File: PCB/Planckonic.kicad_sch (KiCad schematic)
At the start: 127 parts

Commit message: schematic improvements
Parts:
- gave numbers to parts that had none: 127
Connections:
- net col0: now also SW_A9.1, SW_C9.1, U1.5 (2/PD1)
- net col1: now also SW_A10.1, SW_C10.1, U1.6 (3/PD0)
- net col2: now also SW_A11.1, SW_C11.1, U1.7 (4/PD4)
- net col3: now also SW_A12.1, SW_C12.1, U1.8 (5/PC6)
- net col4: now also SW_B9.1, SW_D12.1, SW_E12.1, U1.9 (6/PD7)
- net col5: now also SW_B10.1, SW_D13.1, SW_E13.1, U1.10 (7/PE6)
- net col6: now also SW_B11.1, SW_D14.1, SW_E14.1, U1.11 (8/PB4)
- net col7: now also SW_B12.1, SW_D15.1, SW_E15.1, U1.12 (9/PB5)
- net rowA: now also U1.20 (A3/PF4); no longer D10.2 (A), D11.2 (A), D12.2 (A), D9.2 (A)
- net rowB: now also U1.19 (A2/PF5); no longer D21.2 (A), D22.2 (A), D23.2 (A), D24.2 (A)
- net rowC: now also U1.18 (A1/PF6); no longer D25.2 (A), D34.2 (A), D35.2 (A), D36.2 (A)
- net rowD: now also U1.17 (A0/PF7); no longer D37.2 (A), D38.2 (A), D46.2 (A), D47.2 (A)
- net rowE: now also D10.2 (A), D11.2 (A), D12.2 (A), D21.2 (A), D22.2 (A), D23.2 (A), D24.2 (A), D9.2 (A), U1.16 (15/PB1); no longer D49.2 (A), D50.2 (A), D51.2 (A), D52.2 (A), D53.2 (A), D54.2 (A), D55.2 (A), D56.2 (A), D57.2 (A), D58.2 (A), D59.2 (A), D60.2 (A)
- net rowH: now reaches U1.13 (10/PB6)
- net rowH: now also D49.2 (A), D58.2 (A), D59.2 (A), D60.2 (A)
- net rowG: now reaches U1.14 (16/PB2)
- net rowG: now also D50.2 (A), D51.2 (A), D52.2 (A), D53.2 (A), D54.2 (A), D55.2 (A), D56.2 (A), D57.2 (A)
- net rowF: now reaches U1.15 (14/PB3)
- net rowF: now also D25.2 (A), D34.2 (A), D35.2 (A), D36.2 (A), D37.2 (A), D38.2 (A), D46.2 (A), D47.2 (A)
- net VCC: now reaches U1.21 (VCC)
- net GND: now reaches U1.23 (GND)
- net GND: now also U1.3 (GND), U1.4 (GND)
- removed net col10: SW_A11.1, SW_B11.1, SW_C11.1, SW_D14.1, SW_E14.1
- removed net col11: SW_A12.1, SW_B12.1, SW_C12.1, SW_D15.1, SW_E15.1
- removed net col8: SW_A9.1, SW_B9.1, SW_C9.1, SW_D12.1, SW_E12.1
- removed net col9: SW_A10.1, SW_B10.1, SW_C10.1, SW_D13.1, SW_E13.1
- no-connect marks 0 -> 4
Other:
- moved on the sheet: D10, D11, D12, D21, D22, D23, D24, D25, D34, D35, D36, D37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

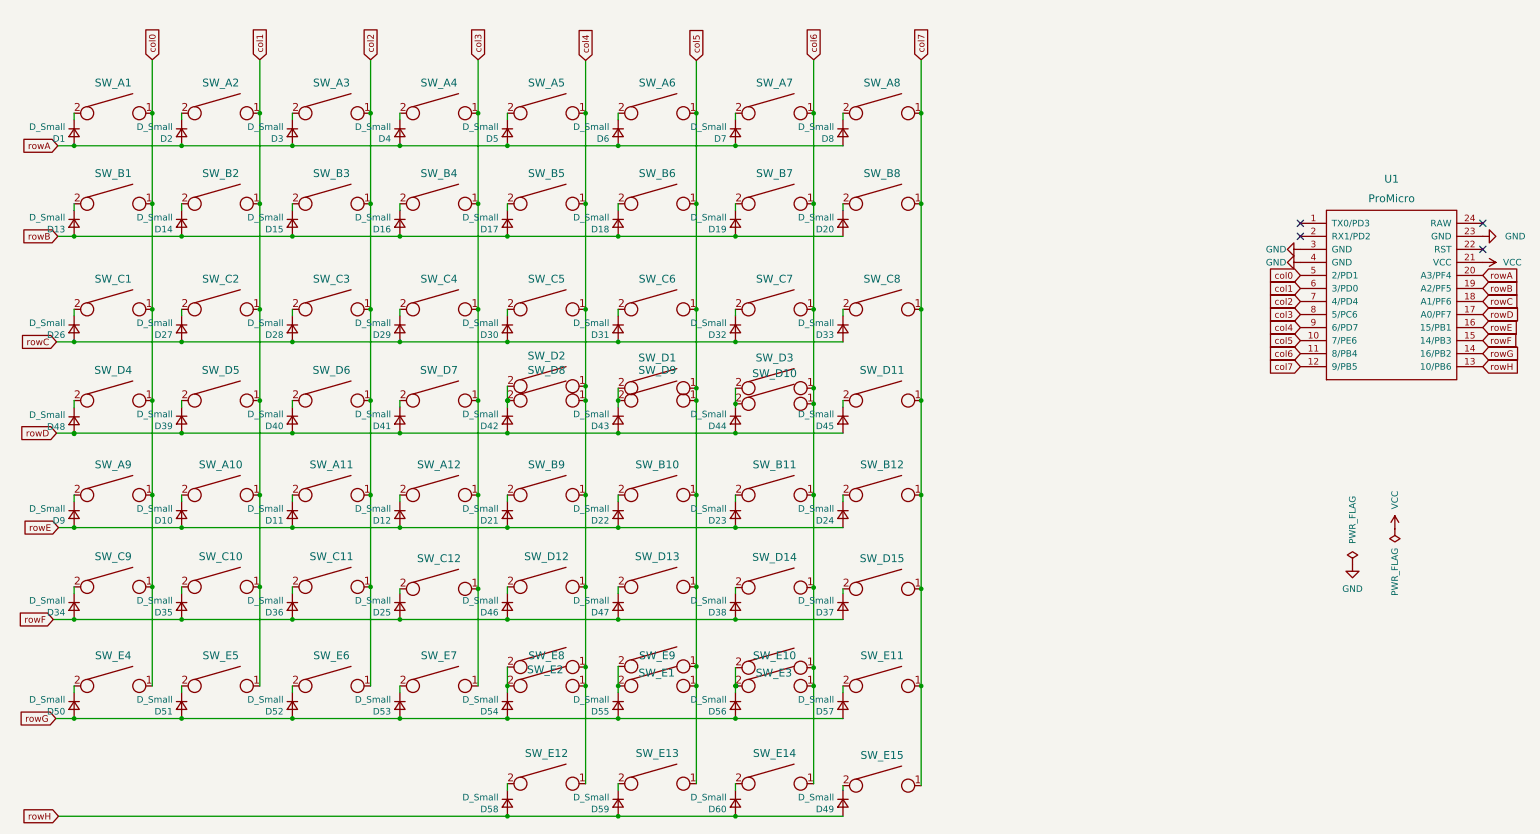
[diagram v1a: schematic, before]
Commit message: schematic done, layout started
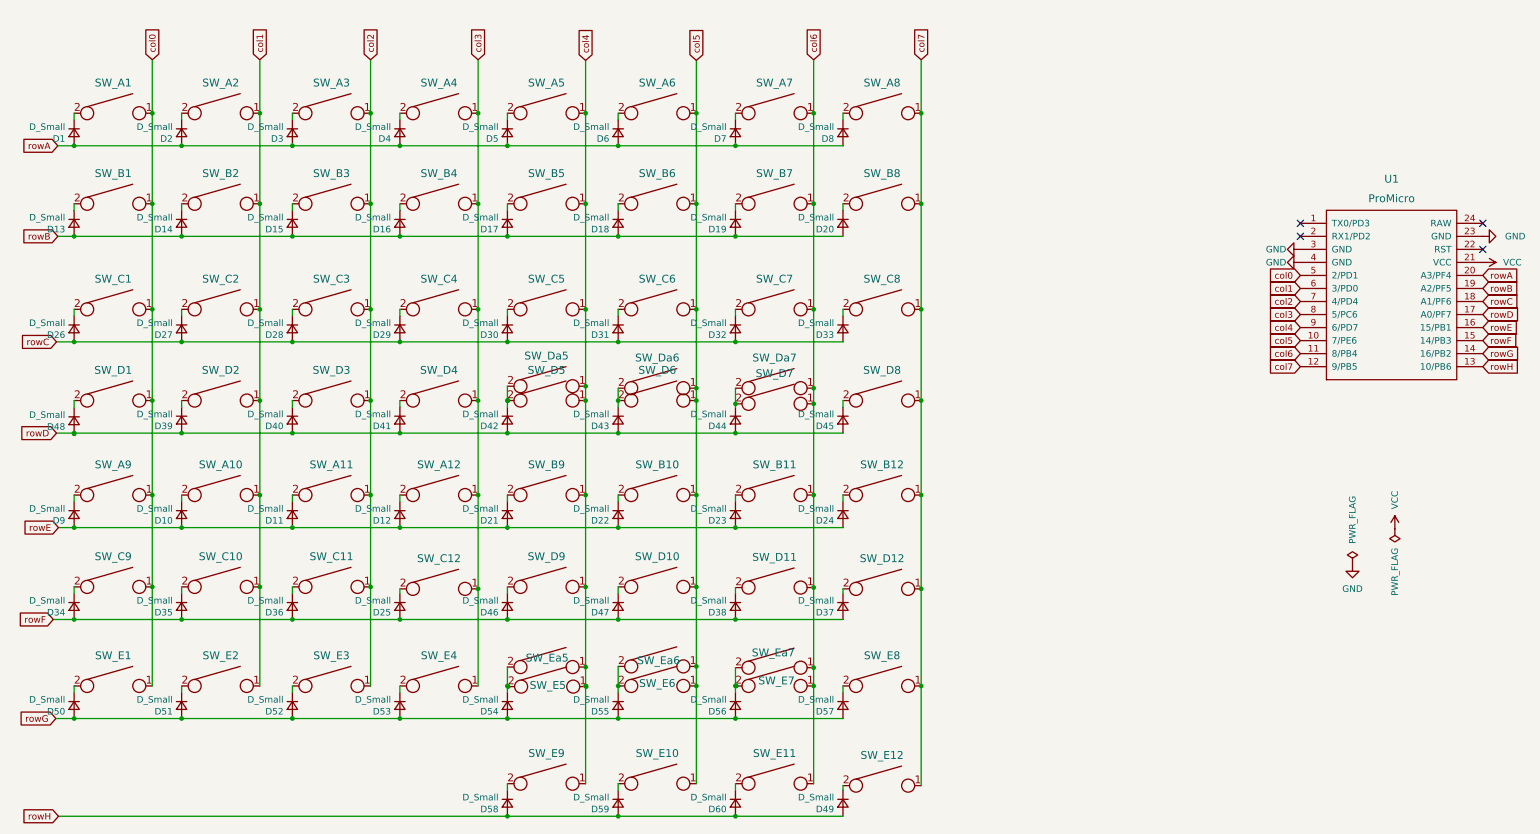
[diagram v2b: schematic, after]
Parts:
- SW_Da5: renamed from SW_D2; footprint Keebio-Parts:MX-Alps-Choc-2U-StabFlip -> Keebio-Parts:MX-Alps-Choc-2U-StabFlip-NoLED
- SW_Da6: renamed from SW_D1; footprint Keebio-Parts:MX-Alps-Choc-2U-StabFlip -> Keebio-Parts:MX-Alps-Choc-2U-StabFlip-NoLED
- SW_Da7: renamed from SW_D3; footprint Keebio-Parts:MX-Alps-Choc-2U-StabFlip -> Keebio-Parts:MX-Alps-Choc-2U-StabFlip-NoLED
- SW_Ea5: renamed from SW_E2; footprint Keebio-Parts:MX-Alps-Choc-2U-StabFlip -> Keebio-Parts:MX-Alps-Choc-2U-StabFlip-NoLED
- SW_Ea6: renamed from SW_E1; footprint Keebio-Parts:MX-Alps-Choc-2U-StabFlip -> Keebio-Parts:MX-Alps-Choc-2U-StabFlip-NoLED
- SW_Ea7: renamed from SW_E3; footprint Keebio-Parts:MX-Alps-Choc-2U-StabFlip -> Keebio-Parts:MX-Alps-Choc-2U-StabFlip-NoLED
- renumbered SW_D4 to SW_D1, SW_D13 to SW_D10, SW_D14 to SW_D11, SW_D15 to SW_D12, SW_D5 to SW_D2, SW_D6 to SW_D3, SW_D7 to SW_D4, SW_D8 to SW_D5, SW_D9 to SW_D6, SW_D10 to SW_D7, SW_D11 to SW_D8, SW_D12 to SW_D9, SW_E4 to SW_E1, SW_E13 to SW_E10, SW_E14 to SW_E11, SW_E15 to SW_E12, SW_E5 to SW_E2, SW_E6 to SW_E3, SW_E7 to SW_E4, SW_E8 to SW_E5, SW_E9 to SW_E6, SW_E10 to SW_E7, SW_E11 to SW_E8, SW_E12 to SW_E9
